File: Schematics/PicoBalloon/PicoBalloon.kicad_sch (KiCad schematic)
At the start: 23 parts, among them J1 ANT, J2 SOLAR_L, J3 SOLAR_R, U1 STM32F103C8Tx, U2 MCP1640Cx-xCHY, U3 BME280

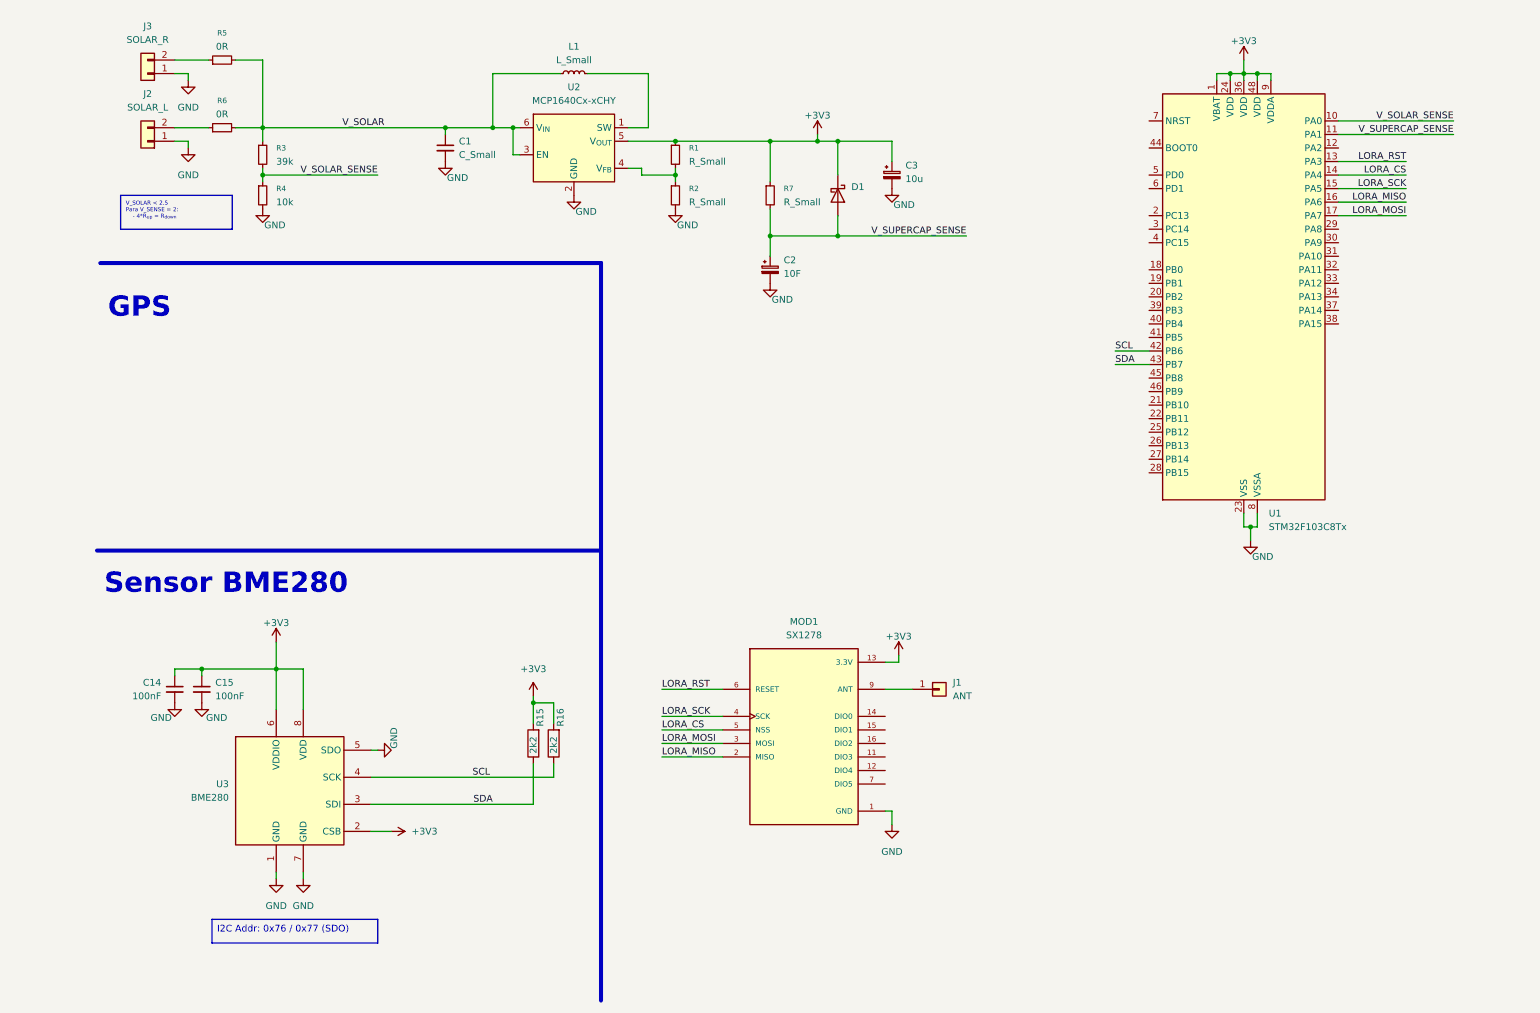
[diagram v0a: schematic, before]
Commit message: GPS v1, BME removed, added temp sensor
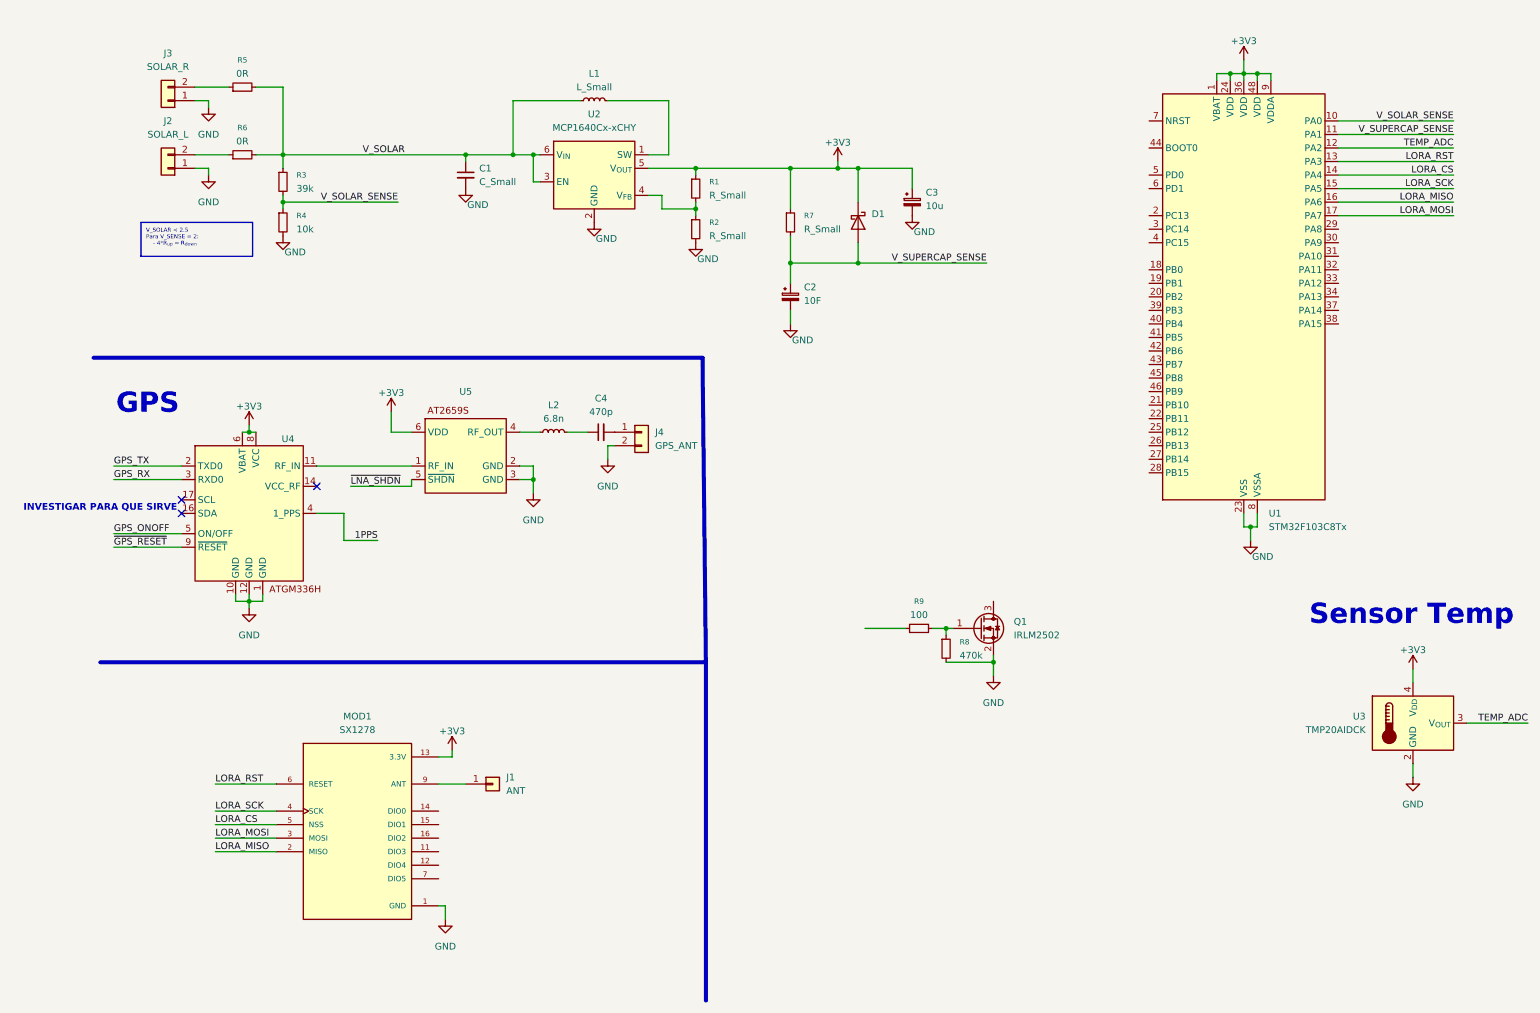
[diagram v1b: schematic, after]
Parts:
- removed C14, C15: 100nF, Capacitor_SMD:C_0603_1608Metric_Pad1.08x0.95mm_HandSolder, symbol Device:C_Small
- removed R15, R16: 2k2, Resistor_SMD:R_0603_1608Metric_Pad0.98x0.95mm_HandSolder, symbol Device:R
- removed U3: BME280, Package_LGA:Bosch_LGA-8_2.5x2.5mm_P0.65mm_ClockwisePinNumbering, symbol Sensor:BME280
- added C4: 470p, symbol Device:C_Small
- added J4: GPS_ANT, symbol Connector_Generic:Conn_01x02
- added L2: 6.8n, Inductor_SMD:L_0805_2012Metric_Pad1.05x1.20mm_HandSolder, symbol Device:L_Small
- added Q1: IRLM2502, Package_TO_SOT_SMD:SOT-23_Handsoldering, symbol Transistor_FET:Q_NMOS_GSD
- added R8: 470k, symbol Device:R_Small
- added R9: 100, symbol Device:R_Small
- added U3: TMP20AIDCK, Package_TO_SOT_SMD:SOT-353_SC-70-5, symbol Sensor_Temperature:TMP20AIDCK
- added U4: ~, symbol gluonLibrary:ATGM336H
- added U5: ~, symbol gluonLibrary:AT2659S
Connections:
- net +3V3: now also U3.4 (V_{DD}), U4.6 (VBAT), U4.8 (VCC), U5.6 (VDD)
- net GND: now also J4.2 (Pin_2), Q1.2 (S), R8.2, U3.2 (GND), U3.5 (GND), U4.1 (GND), U4.10 (GND), U4.12 (GND), U5.2 (GND), U5.3 (GND)
- net TEMP_ADC: now reaches U1.12 (PA2)
- net TEMP_ADC: now also U3.3 (V_{OUT})
- net SCL: no longer names the net of U1.42 (PB6)
- net SDA: no longer names the net of U1.43 (PB7)
- new net: Q1.1 (G), R8.1, R9.2
- new net: U4.11 (RF_IN), U5.1 (RF_IN)
- new net: C4.1, L2.2
- new net: C4.2, J4.1 (Pin_1)
- new net: L2.1, U5.4 (RF_OUT)
- new net 1PPS: U4.4 (1_PPS)
- new net GPS_ONOFF: U4.5 (ON/OFF)
- new net GPS_RX: U4.3 (RXD0)
- new net GPS_TX: U4.2 (TXD0)
- new net ~{GPS_RESET}: U4.9 (~{RESET})
- new net ~{LNA_SHDN}: U5.5 (~{SHDN})
- no-connect marks 0 -> 3
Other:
- note added: "INVESTIGAR PARA QUE SIRVE"
- note added: "Sensor Temp"
- note removed: "Sensor BME280"
- moved on the sheet: C1, C2, C3, D1, J1, J2, J3, L1, MOD1, R1, R2, R3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

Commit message: Updated Schematics for the Boost
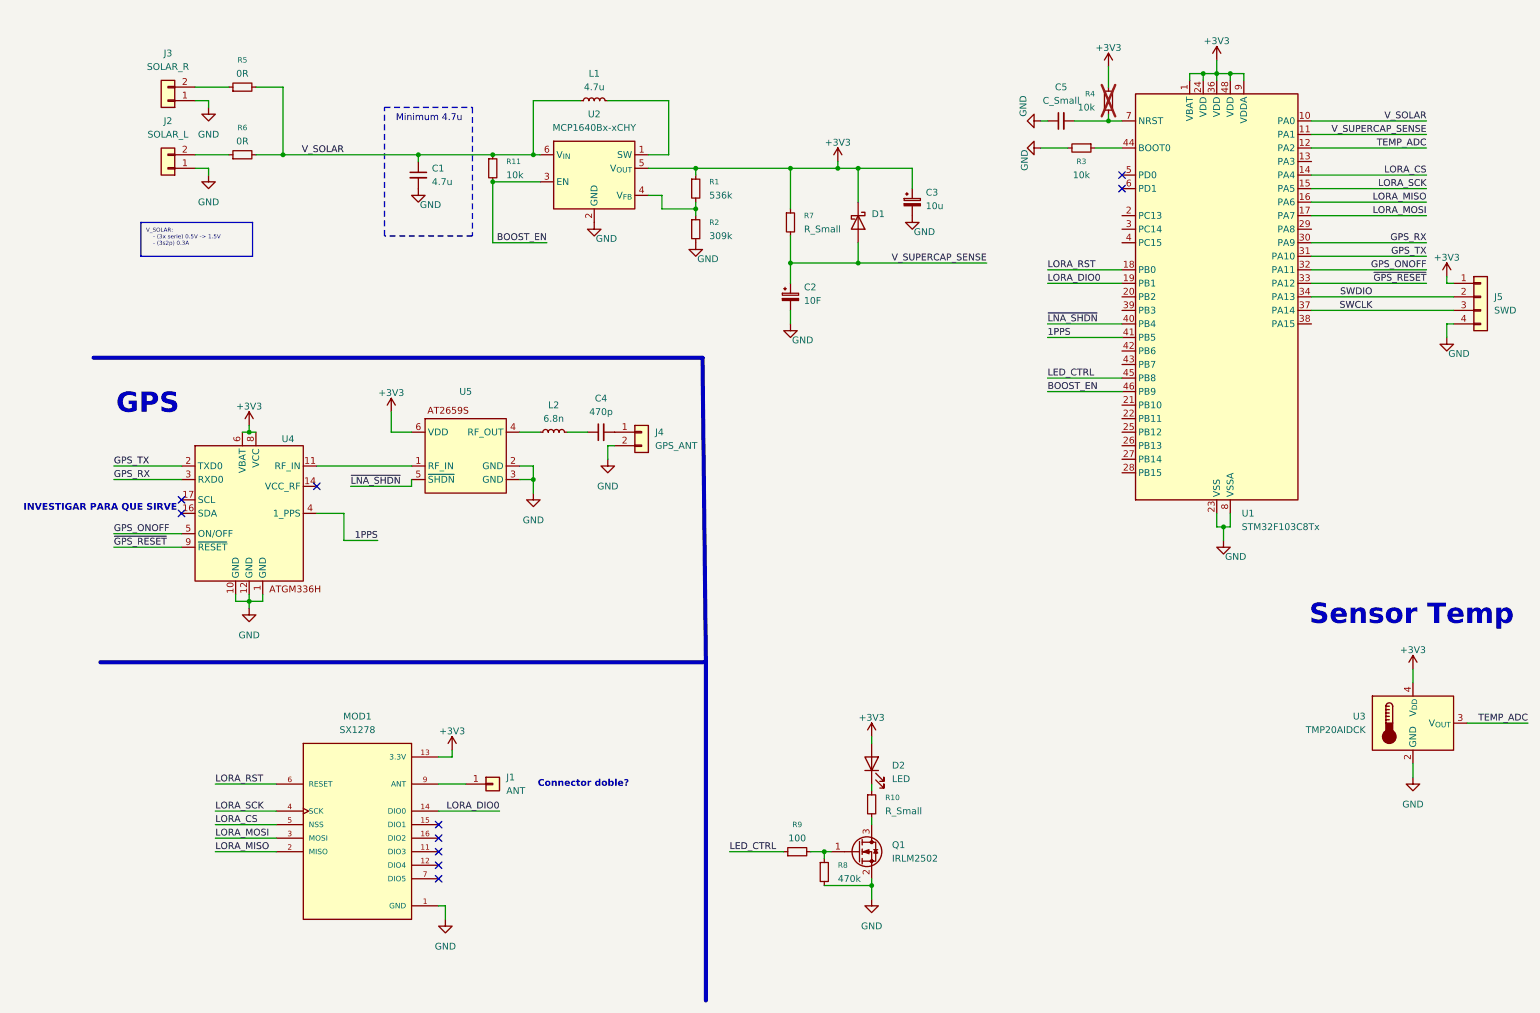
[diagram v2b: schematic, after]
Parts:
- added C5: C_Small, symbol Device:C_Small
- added D2: LED, symbol Device:LED
- added J5: SWD, symbol Connector_Generic:Conn_01x04
- added R10: R_Small, symbol Device:R_Small
- added R11: 10k, symbol Device:R_Small
- C1: value C_Small -> 4.7u
- L1: value L_Small -> 4.7u; footprint (none) -> Inductor_SMD:L_1008_2520Metric_Pad1.43x2.20mm_HandSolder; LCSC (none) -> https://lcsc.com/product-detail/Power-Inductors_INPAQ-WIP25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
- R1: value R_Small -> 536k; footprint (none) -> Resistor_SMD:R_0805_2012Metric_Pad1.20x1.40mm_HandSolder
- R2: value R_Small -> 309k; footprint (none) -> Resistor_SMD:R_0805_2012Metric_Pad1.20x1.40mm_HandSolder
- R3: value 39k -> 10k
- R4: now not fitted
- U2: value MCP1640Cx-xCHY -> MCP1640Bx-xCHY
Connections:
- net +3V3: now also R4.1, D2.2 (A), J5.1 (Pin_1)
- net 1PPS: now also U1.41 (PB5)
- net GND: now also R3.2, C5.1, J5.4 (Pin_4); no longer R4.2
- net GPS_ONOFF: now also U1.32 (PA11)
- net GPS_RX: now also U1.30 (PA9)
- net GPS_TX: now also U1.31 (PA10)
- net LORA_RST: now also U1.18 (PB0); no longer U1.13 (PA3)
- net V_SOLAR: now also U1.10 (PA0), R11.1; no longer R3.1, U2.3 (EN)
- net ~{GPS_RESET}: now also U1.33 (PA12)
- net ~{LNA_SHDN}: now also U1.40 (PB4)
- net at Q1.3 (D): now also R10.2
- net LED_CTRL: now reaches R9.1
- net LED_CTRL: now also U1.45 (PB8)
- net LORA_DIO0: now reaches MOD1.14 (DIO0)
- net LORA_DIO0: now also U1.19 (PB1)
- net SWDIO: now reaches U1.34 (PA13)
- net SWDIO: now also J5.2 (Pin_2)
- net SWCLK: now reaches U1.37 (PA14)
- net SWCLK: now also J5.3 (Pin_3)
- net at U1.44 (BOOT0): now also R3.1
- net BOOST_EN: now reaches U1.46 (PB9)
- net BOOST_EN: now also U2.3 (EN), R11.2
- net at U1.7 (NRST): now also R4.2, C5.2
- removed net V_SOLAR_SENSE: R3.2, R4.1, U1.10 (PA0)
- new net: D2.1 (K), R10.1
- no-connect marks 3 -> 10
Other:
- note added: "Connector doble?"
- note added: "Minimum 4.7u"
- moved on the sheet: C1, Q1, R8, R9, U1

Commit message: Finished schematic V1
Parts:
- removed C1: 4.7u, symbol Device:C_Small
- removed C2: 10F, symbol Device:C_Polarized_Small
- removed C3: 10u, symbol Device:C_Polarized_Small
- removed D1: D_Schottky, symbol Device:D_Schottky
- removed D2: LED, symbol Device:LED
- removed J1: ANT, symbol Connector_Generic:Conn_01x01
- removed L1: 4.7u, Inductor_SMD:L_1008_2520Metric_Pad1.43x2.20mm_HandSolder, symbol Device:L_Small
- removed Q1: IRLM2502, Package_TO_SOT_SMD:SOT-23_Handsoldering, symbol Transistor_FET:Q_NMOS_GSD
- removed R1: 536k, Resistor_SMD:R_0805_2012Metric_Pad1.20x1.40mm_HandSolder, symbol Device:R_Small
- removed R10, R7: R_Small, symbol Device:R_Small
- removed R11: 10k, symbol Device:R_Small
- removed R2: 309k, Resistor_SMD:R_0805_2012Metric_Pad1.20x1.40mm_HandSolder, symbol Device:R_Small
- removed R8: 470k, symbol Device:R_Small
- removed R9: 100, symbol Device:R_Small
- removed U2: MCP1640Bx-xCHY, Package_TO_SOT_SMD:SOT-23-6, symbol Regulator_Switching:MCP1640Cx-xCHY
- added AE1: W3011, RF_Antenna:Pulse_W3011, symbol Device:Antenna
- added C10: 10u, Capacitor_SMD:C_0805_2012Metric_Pad1.18x1.45mm_HandSolder, symbol Device:C_Small
- added C11, C12, C13, C14, C15, C6, C7, C8, C9: 100n, Capacitor_SMD:C_0603_1608Metric_Pad1.08x0.95mm_HandSolder, symbol Device:C_Small
- added D3, D4: LED, LED_SMD:LED_0603_1608Metric_Pad1.05x0.95mm_HandSolder, symbol Device:LED
- added R12, R13: 1k, Resistor_SMD:R_0603_1608Metric_Pad0.98x0.95mm_HandSolder, symbol Device:R_Small
- C4: footprint (none) -> Capacitor_SMD:C_0603_1608Metric_Pad1.08x0.95mm_HandSolder; LCSC (none) -> https://lcsc.com/product-detail/Multilayer-Ceramic-Capacito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
- C5: value C_Small -> 100n; footprint (none) -> Capacitor_SMD:C_0603_1608Metric_Pad1.08x0.95mm_HandSolder; LCSC (none) -> https://lcsc.com/product-detail/Multilayer-Ceramic-Capacito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
- J2, J3: footprint (none) -> Connector_PinHeader_2.00mm:PinHeader_1x02_P2.00mm_Vertical
- J4: value GPS_ANT -> LORA_ANT; footprint (none) -> Connector_PinHeader_2.00mm:PinHeader_1x02_P2.00mm_Vertical
- J5: footprint (none) -> Connector_PinHeader_2.54mm:PinHeader_1x04_P2.54mm_Vertical
- L2: footprint Inductor_SMD:L_0805_2012Metric_Pad1.05x1.20mm_HandSolder -> Inductor_SMD:L_0603_1608Metric_Pad1.05x0.95mm_HandSolder; LCSC https://lcsc.com/product-detail/Inductors-SMD_FH-VHF201209H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 -> https://lcsc.com/product-detail/Inductors-SMD_HYHONGYEX-HBL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
- R3, R4, R5, R6: footprint (none) -> Resistor_SMD:R_0603_1608Metric_Pad0.98x0.95mm_HandSolder
- U3: value TMP20AIDCK -> TMP235A4DCKR; LCSC (none) -> https://lcsc.com/product-detail/Temperature-Sensors_TI-TMP2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
- U5: LCSC (none) -> https://lcsc.com/product-detail/Low-Noise-Amplifiers-LNA-RF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
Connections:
- net +3V3: now also C10.1, C11.2, C12.2, C13.2, C14.2, C6.2, C7.2, C8.2, C9.2, D3.2 (A), D4.2 (A)
- net GND: now also C10.2, C11.1, C12.1, C13.1, C14.1, C15.1, C6.1, C7.1, C8.1, C9.1
- net TEMP_ADC: now also C15.2
- net at MOD1.9 (ANT): now also J4.1 (Pin_1)
- net at C4.2: now also AE1.1 (A); no longer J4.1 (Pin_1)
- net at U1.26 (PB13): now also R12.2
- net at U1.27 (PB14): now also R13.2
- net LED_CTRL renamed SUPERCAP_EN
- new net: D4.1 (K), R13.1
- new net: D3.1 (K), R12.1
- no-connect marks 10 -> 24
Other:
- added sheet Power (power.kicad_sch)
- note added: "LORA"
- note removed: "Connector doble?"
- note removed: "INVESTIGAR PARA QUE SIRVE"
- note removed: "Minimum 4.7u"
- moved on the sheet: C5, J2, J3, J5, R3, R4, R5, R6, U1, U3, U4
